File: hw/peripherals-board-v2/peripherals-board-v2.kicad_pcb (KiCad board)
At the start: 2 copper layers, 75 x 55 mm, 16 parts

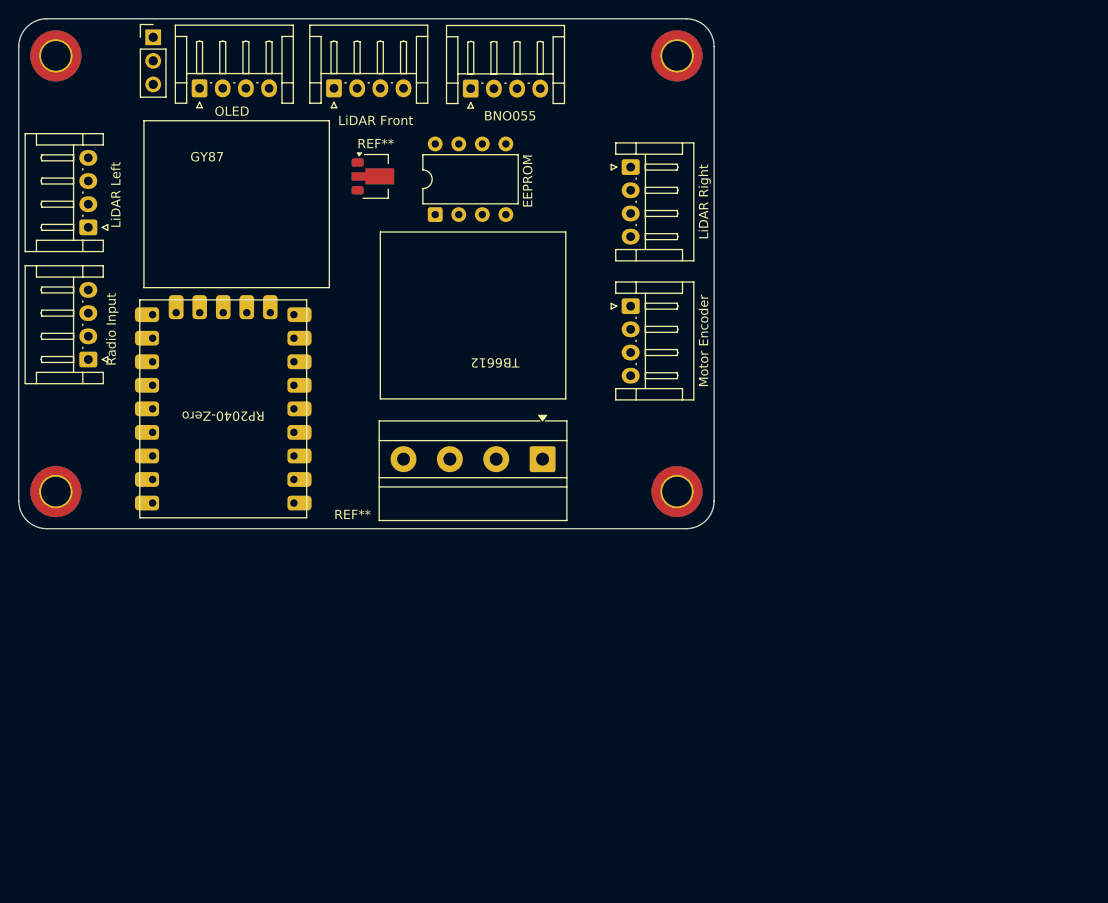
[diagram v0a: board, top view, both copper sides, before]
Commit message: Revision 1 of PCB layout, create footprints, generate interactive BOM
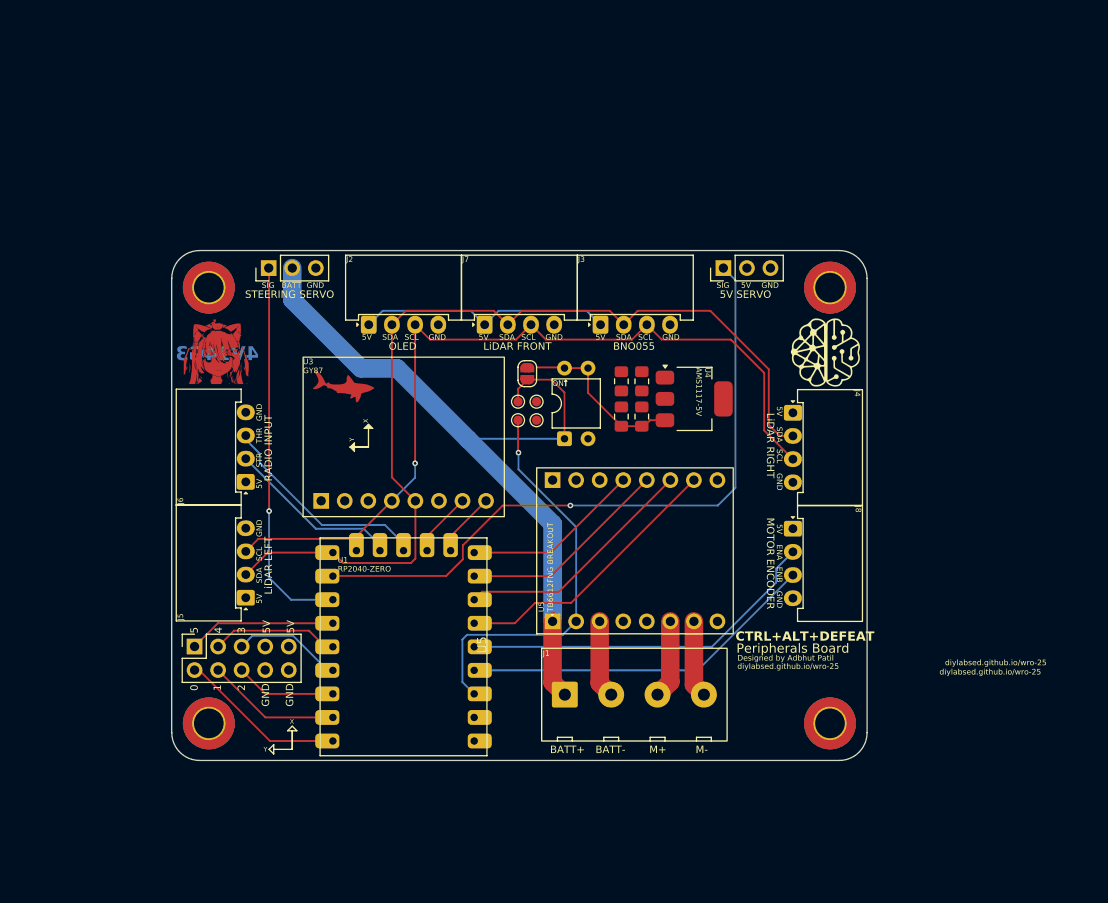
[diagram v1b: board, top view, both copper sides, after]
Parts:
- removed BNO055, OLED: JST_EH_S4B-EH_1x04_P2.50mm_Horizontal, Connector_JST:JST_EH_S4B-EH_1x04_P2.50mm_Horizontal
- removed EEPROM: DIP-8_W7.62mm, Package_DIP:DIP-8_W7.62mm
- removed LiDAR Front: JST_EH_S4B-EH_1x04_P2.50mm_Horizontal, Connector_JST:JST_EH_S4B-EH_1x04_P2.50mm_Horizontal
- removed LiDAR Left: JST_EH_S4B-EH_1x04_P2.50mm_Horizontal, Connector_JST:JST_EH_S4B-EH_1x04_P2.50mm_Horizontal
- removed LiDAR Right: JST_EH_S4B-EH_1x04_P2.50mm_Horizontal, Connector_JST:JST_EH_S4B-EH_1x04_P2.50mm_Horizontal
- removed Motor Encoder: JST_EH_S4B-EH_1x04_P2.50mm_Horizontal, Connector_JST:JST_EH_S4B-EH_1x04_P2.50mm_Horizontal
- removed the REF** at (26.5, 73.0)
- removed the REF** at (93.5, 73.0)
- removed the REF** at (93.5, 26.0)
- removed the REF** at (26.5, 26.0)
- removed the REF** at (61.0, 39.0)
- removed the REF** at (79.0, 69.5)
- removed the REF** at (54.7, 51.4)
- removed Radio Input: JST_EH_S4B-EH_1x04_P2.50mm_Horizontal, Connector_JST:JST_EH_S4B-EH_1x04_P2.50mm_Horizontal
- removed Steering Servo: PinHeader_1x03_P2.54mm_Vertical, Connector_PinHeader_2.54mm:PinHeader_1x03_P2.54mm_Vertical
- added C1: 0.1 uF, Capacitor_SMD:C_0805_2012Metric_Pad1.18x1.45mm_HandSolder, F.Cu at (87.5, 64.9)
- added C2: 0.1 uF, Capacitor_SMD:C_0805_2012Metric_Pad1.18x1.45mm_HandSolder, F.Cu at (87.5, 61.1)
- added C3: 10 uF, Capacitor_SMD:C_0805_2012Metric_Pad1.18x1.45mm_HandSolder, F.Cu at (89.7, 64.9)
- added C4: 10 uF, Capacitor_SMD:C_0805_2012Metric_Pad1.18x1.45mm_HandSolder, F.Cu at (89.7, 61.1)
- added G***: LOGO, LOGO, F.Cu at (57.4, 61.6)
- added G***: LOGO, LOGO, F.Cu at (109.5, 58.0)
- added G***: LOGO, LOGO, F.Cu at (43.8, 57.9)
- added G***: LOGO, LOGO, B.Cu at (89.4, 63.5)
- added G***: LOGO, LOGO, B.Cu at (99.5, 63.5)
- added G***: LOGO, LOGO, B.Cu at (89.0, 79.4)
- added J1: Power/Motor Screw Terminal, ScrewTerminal_01x04_P5mm:ScrewTerminal_01x04_P5mm, F.Cu at (86.2, 104.3)
- added J10: Extra Servo, Connector_PinHeader_2.54mm:PinHeader_1x03_P2.54mm_Vertical, F.Cu at (98.5, 48.9)
- added J11: Conn_02x05_Odd_Even, Connector_PinSocket_2.54mm:PinSocket_2x05_P2.54mm_Vertical, F.Cu at (41.5, 89.7)
- added J2: OLED, JST_XH_01x04_Horizontal_NoFlange:JST_XH_01x04_Horizontal_NoFlange, F.Cu at (60.2, 55.0)
- added J3: BNO055, JST_XH_01x04_Horizontal_NoFlange:JST_XH_01x04_Horizontal_NoFlange, F.Cu at (85.2, 55.0)
- added J4: LiDAR Right, JST_XH_01x04_Horizontal_NoFlange:JST_XH_01x04_Horizontal_NoFlange, F.Cu at (106.0, 64.5)
- added J5: LiDAR Left, JST_XH_01x04_Horizontal_NoFlange:JST_XH_01x04_Horizontal_NoFlange, F.Cu at (47.0, 84.5)
- added J6: Radio Input, JST_XH_01x04_Horizontal_NoFlange:JST_XH_01x04_Horizontal_NoFlange, F.Cu at (47.0, 72.0)
- added J7: LiDAR Front, JST_XH_01x04_Horizontal_NoFlange:JST_XH_01x04_Horizontal_NoFlange, F.Cu at (72.8, 55.0)
- added J8: Motor Encoder, JST_XH_01x04_Horizontal_NoFlange:JST_XH_01x04_Horizontal_NoFlange, F.Cu at (106.0, 77.0)
- added J9: Steering Servo, Connector_PinHeader_2.54mm:PinHeader_1x03_P2.54mm_Vertical, F.Cu at (49.5, 48.9)
- added JP1: SW1 Bypass, Jumper:SolderJumper-2_P1.3mm_Open_RoundedPad1.0x1.5mm, F.Cu at (77.3, 60.3)
- added ON: Power, Package_DIP:DIP-4_W7.62mm, F.Cu at (81.4, 67.3)
- added REF**: MountingHole_3.2mm_M3_DIN965_Pad_TopBottom, MountingHole:MountingHole_3.2mm_M3_DIN965_Pad_TopBottom, F.Cu at (43.0, 51.0)
- added REF**: MountingHole_3.2mm_M3_DIN965_Pad_TopBottom, MountingHole:MountingHole_3.2mm_M3_DIN965_Pad_TopBottom, F.Cu at (110.0, 98.0)
- added REF**: MountingHole_3.2mm_M3_DIN965_Pad_TopBottom, MountingHole:MountingHole_3.2mm_M3_DIN965_Pad_TopBottom, F.Cu at (110.0, 51.0)
- added REF**: MountingHole_3.2mm_M3_DIN965_Pad_TopBottom, MountingHole:MountingHole_3.2mm_M3_DIN965_Pad_TopBottom, F.Cu at (43.0, 98.0)
- added TP1: GND, TestPoint:TestPoint_Pad_D1.0mm, F.Cu at (78.3, 65.3)
- added TP2: +5V, TestPoint:TestPoint_Pad_D1.0mm, F.Cu at (78.3, 63.3)
- added TP3: +3.3V, TestPoint:TestPoint_Pad_D1.0mm, F.Cu at (76.3, 65.3)
- added TP4: +BATT, TestPoint:TestPoint_Pad_D1.0mm, F.Cu at (76.3, 63.3)
- added U1: RP2040-Zero, RP2040-Zero:RP2040-Zero, F.Cu at (74.2, 77.0)
- added U3: ~, GY87:GY87, F.Cu at (65.2, 71.2)
- added U4: AMS1117-5.0, Package_TO_SOT_SMD:SOT-223-3_TabPin2, F.Cu at (95.3, 63.0)
- added U5: ~, TB6612FNG-breakout:TB6612FNG-breakout, F.Cu at (80.1, 92.1)
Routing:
- net /I2C0_SDA: track 0.00 -> 101.7 mm
- net /I2C0_SCL: track 0.00 -> 94.3 mm, vias 0 -> 1
- net +BATT: track 0.00 -> 85.7 mm
- net /EXT_SERVO: track 0.00 -> 72.5 mm, vias 0 -> 1
- net +3.3V: track 0.00 -> 43.8 mm, vias 0 -> 1
- net /STR_SERVO: track 0.00 -> 41.3 mm, vias 0 -> 1
- net /ENCA: track 0.00 -> 39.5 mm
- net /ENCB: track 0.00 -> 38.6 mm
- net /PWMB: track 0.00 -> 30.1 mm
- net +5V: track 0.00 -> 27.5 mm
- net /BIN2: track 0.00 -> 26.5 mm
- net /RX_THR: track 0.00 -> 24.1 mm
- net /BIN1: track 0.00 -> 22.9 mm
- net /STBY: track 0.00 -> 19.3 mm
- net /RX_STR: track 0.00 -> 18.9 mm
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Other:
- board text added: "0"
- board text added: "1"
- board text added: "2"
- board text added: "3"
- board text added: "4"
- board text added: "4V14G3"
- board text added: "5"
- board text added: "5V"
- board text added: "5V SERVO"
- board text added: "BATT"
- board text added: "BATT+"
- board text added: "BATT-"
- board text added: "BNO055"
- board text added: "CTRL+ALT+DEFEAT"
- board text added: "Designed by Adbhut Patil"
- board text added: "ENA"
- board text added: "ENB"
- board text added: "GND"
- board text added: "GitHub Repo"
- board text added: "J1"
- board text added: "J2"
- board text added: "J3"
- board text added: "J4"
- board text added: "J5"
- board text added: "J6"
- board text added: "J7"
- board text added: "J8"
- board text added: "LiDAR FRONT"
- board text added: "LiDAR LEFT"
- board text added: "LiDAR RIGHT"
- board text added: "M+"
- board text added: "M-"
- board text added: "MOTOR ENCODER"
- board text added: "OLED"
- board text added: "ON"
- board text added: "Peripherals Board"
- board text added: "Peripherals Interface Board"
- board text added: "RADIO INPUT"
- board text added: "SCL"
- board text added: "SDA"
- board text added: "SIG"
- board text added: "STEERING SERVO"
- board text added: "STR"
- board text added: "THR"
- board text added: "U1 RP2040-ZERO"
- board text added: "U3 GY87"
- board text added: "U4 AMS1117-5V"
- board text added: "U5 TB6612FNG BREAKOUT"
- board text added: "Website"
- board text added: "X"
- board text added: "Y"
- board text added: "diylabsed.github.io/wro-25"
- board text added: "https://DIYLabsED.GitHub.io/wro-25"
- board text removed: "GY87"
- board text removed: "TB6612"

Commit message: Change URL to lowercase
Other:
- board text added: "https://diylabsed.github.io/wro-25"
- board text removed: "https://DIYLabsED.GitHub.io/wro-25"
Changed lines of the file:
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@@
-		)
-	)
-	(gr_text "diylabsed.github.io/wro-25"
-		(at 121.8 92.8 0)
-		(layer "F.SilkS")
-		(effects
-			(font
-				(size 0.6 0.6)
-				(thickness 0.075)
-			)
-			(justify left bottom)
 		)
 	)
@@
 				(size 0.6 0.6)
 				(thickness 0.1)
-			)
-			(justify left bottom)
-		)
-	)
-	(gr_text "diylabsed.github.io/wro-25"
-		(at 122.4 91.8 0)
-		(layer "F.SilkS")
-		(effects
-			(font
-				(size 0.6 0.6)
-				(thickness 0.075)
 			)
 			(justify left bottom)
@@
 		)
 	)
-	(gr_text "https://DIYLabsED.GitHub.io/wro-25\n"
+	(gr_text "https://diylabsed.github.io/wro-25\n"
 		(at 79.8 67.5 0)
 		(layer "B.SilkS")
@@
 	(group ""
 		(members "57b87c6b-6795-4c16-813f-7b25c02e8e27" "8be86143-ee16-4ab6-84d1-f07a21c35082"
-			"bc0e079f-9c5e-4db5-99b2-6822604a57ec" "d07d6b22-6a29-4d67-b3b7-077e6eceaa15"
-		)
-	)
+			"bc0e079f-9c5e-4db5-99b2-6822604a57ec"
+		)
+	)

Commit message: Create fill both layers for 5v and GND
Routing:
- net +5V: track 27.5 -> 51.7 mm
- net GND: track 8.41 -> 30.5 mm
- added copper zone on F.Cu, net +5V
- added copper zone on B.Cu, net GND
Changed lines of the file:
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@@
+	)
+	(segment
+		(start 52.87 93.5)
+		(end 51.62 92.25)
+		(width 0.2)
+		(layer "B.Cu")
+		(net 1)
+	)
+	(segment
+		(start 71.62 97.36)
+		(end 67.76 93.5)
+		(width 0.2)
+		(layer "B.Cu")
+		(net 1)
+	)
+	(segment
+		(start 67.76 93.5)
+		(end 52.87 93.5)
+		(width 0.2)
+		(layer "B.Cu")
+		(net 1)
 	)
 	(segment
@@
 		(layer "B.Cu")
 		(net 2)
+	)
+	(segment
+		(start 66.3 99.9)
+		(end 57.4 91)
+		(width 0.2)
+		(layer "F.Cu")
+		(net 3)
+	)
+	(segment
+		(start 57.4 91)
+		(end 52.91 91)
+		(width 0.2)
+		(layer "F.Cu")
+		(net 3)
+	)
+	(segment
+		(start 52.91 91)
+		(end 51.62 89.71)
+		(width 0.2)
+		(layer "F.Cu")
+		(net 3)
+	)
+	(segment
+		(start 71.62 99.9)
+		(end 66.3 99.9)
+		(width 0.2)
+		(layer "F.Cu")
+		(net 3)
 	)
 	(segment
@@
 		(layer "F.Cu")
 		(net 34)
+	)
+	(zone
+		(net 3)
+		(net_name "+5V")
+		(layer "F.Cu")
+		(hatch edge 0.5)
+		(connect_pads yes
+			(clearance 0.5)
+		)
+		(min_thickness 0.5)
+		(filled_areas_thickness no)
+		(fill yes
+			(thermal_gap 0.5)
+			(thermal_bridge_width 0.5)
+		)
+		(polygon
+			(pts
+				(xy 120 40) (xy 120 105) (xy 30 105) (xy 30 40)
+			)
+		)
 	)
 	(zone
@@
 		(polygon
 			(pts
-				(xy 61 59.8) (xy 61.1 59.9) (xy 61.1 63.5) (xy 54.1 63.5) (xy 54.1 59.8)
+				(xy 61.1 59) (xy 61.5 59) (xy 61.5 64.1) (xy 53.4 64.1) (xy 53.4 59)
 			)
 		)
@@
 		(layer "F.Cu")
 		(hatch edge 0.5)
-		(connect_pads
+		(connect_pads yes
 			(clearance 0)
 		)
@@
 		(polygon
 			(pts
-				(xy 43.6993 54.42276) (xy 46.5 54.42276) (xy 46.5 57.4) (xy 46.509965 57.409965) (xy 46.7 57.409965)
-				(xy 47.300597 58.010562) (xy 47.300597 61.342052) (xy 47.242649 61.4) (xy 40.3 61.4) (xy 40.3 57.7)
-				(xy 41.2 56.8) (xy 41.2 54.9) (xy 42.9 54.9) (xy 43.4 54.4) (xy 43.7 54.4) (xy 43.7 54.42206)
+				(xy 47.7 54.4) (xy 47.8 54.5) (xy 47.8 61.5) (xy 39.9 61.5) (xy 39.9 54.4) (xy 43.6 54.4)
 			)
 		)
+	)
+	(zone
+		(net 1)
+		(net_name "GND")
+		(layer "B.Cu")
+		(hatch edge 0.5)
+		(priority 1)
+		(connect_pads yes
+			(clearance 0.5)
+		)
+		(min_thickness 0.5)
+		(filled_areas_thickness no)
+		(fill yes
+			(thermal_gap 0.5)
+			(thermal_bridge_width 0.5)
+		)
+		(polygon
+			(pts
+				(xy 30 40) (xy 120 40) (xy 120 105) (xy 30 105)
+			)
+		)

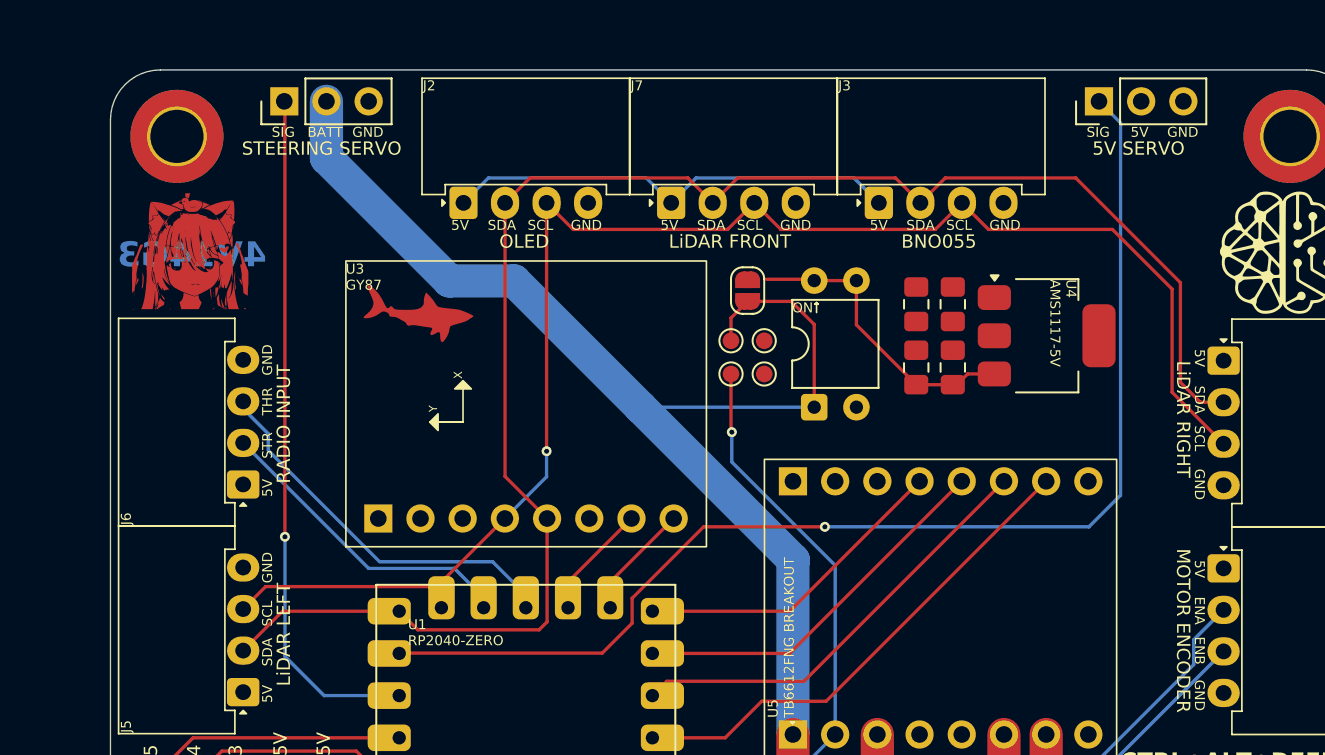
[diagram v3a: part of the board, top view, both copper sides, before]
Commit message: Routing changes to connect vreg to 5v plane
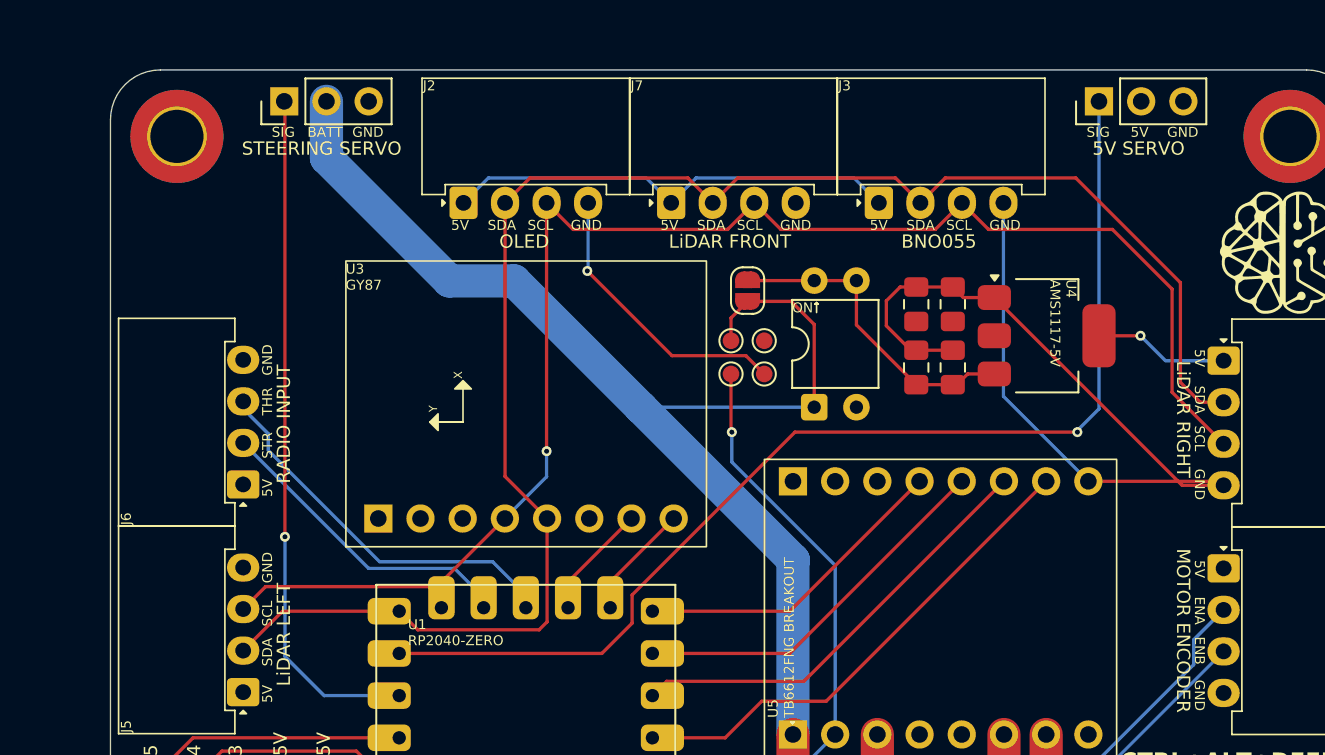
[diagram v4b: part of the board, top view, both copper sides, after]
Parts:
- removed the G*** at (57.4, 61.6)
- removed the G*** at (43.8, 57.9)
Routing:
- net GND: track 30.5 -> 107.0 mm, vias 0 -> 1
- net +5V: track 51.7 -> 59.8 mm, vias 0 -> 1
- net /EXT_SERVO: track 72.5 -> 67.8 mm
- net Net-(JP1-B): track 18.2 -> 19.3 mm
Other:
- board text removed: "4V14G3"

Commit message: Reroute PCB
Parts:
- moved U3 8.54 mm to (62.8, 63.0), turned to -90 degrees
- renumbered ON to SW1
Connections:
- U1 pad 13: /INT1 -> /DRDY
- U1 pad 14: /DRDY -> /INT1
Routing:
- net GND: track 107.0 -> 87.8 mm, vias 1 -> 2
- net /INT1: track 6.95 -> 23.9 mm, vias 0 -> 1
- net /DRDY: track 6.95 -> 23.9 mm, vias 0 -> 1
- net /EXT_SERVO: track 67.8 -> 81.4 mm, vias 1 -> 0
- net +5V: track 59.8 -> 49.6 mm
- net /I2C0_SDA: track 101.7 -> 95.1 mm
- net +3.3V: track 43.8 -> 48.0 mm
- net +BATT: track 85.7 -> 89.2 mm
- net /STR_SERVO: track 41.3 -> 38.8 mm, vias 1 -> 0
- net /I2C0_SCL: track 94.3 -> 92.2 mm, vias 1 -> 0
- net /ENCB: track 38.6 -> 40.4 mm
- net /RX_THR: track 24.1 -> 22.4 mm
- net /ENCA: track 39.5 -> 40.7 mm
- net /GP3: track 11.9 -> 10.9 mm
- net /RX_STR: track 18.9 -> 19.5 mm
- added copper zone on B.Cu, net +5V
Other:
- board text removed: "Peripherals Board"
- board text removed: "diylabsed.github.io/wro-25"
